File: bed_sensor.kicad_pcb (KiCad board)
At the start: 2 copper layers, 41 x 36 mm, 32 parts, among them J1 Conn_01x02, J2 Conn_01x06, J3 ISP, J4 Conn_01x02, Q1 2N2219, SW1 SW_SPST, U1 MIC5205-3.3, U2 MPU-9250, U5 CFAH0802D-YYH-JP, U6 ATMEGA328-AU, Y1 Crystal_GND2

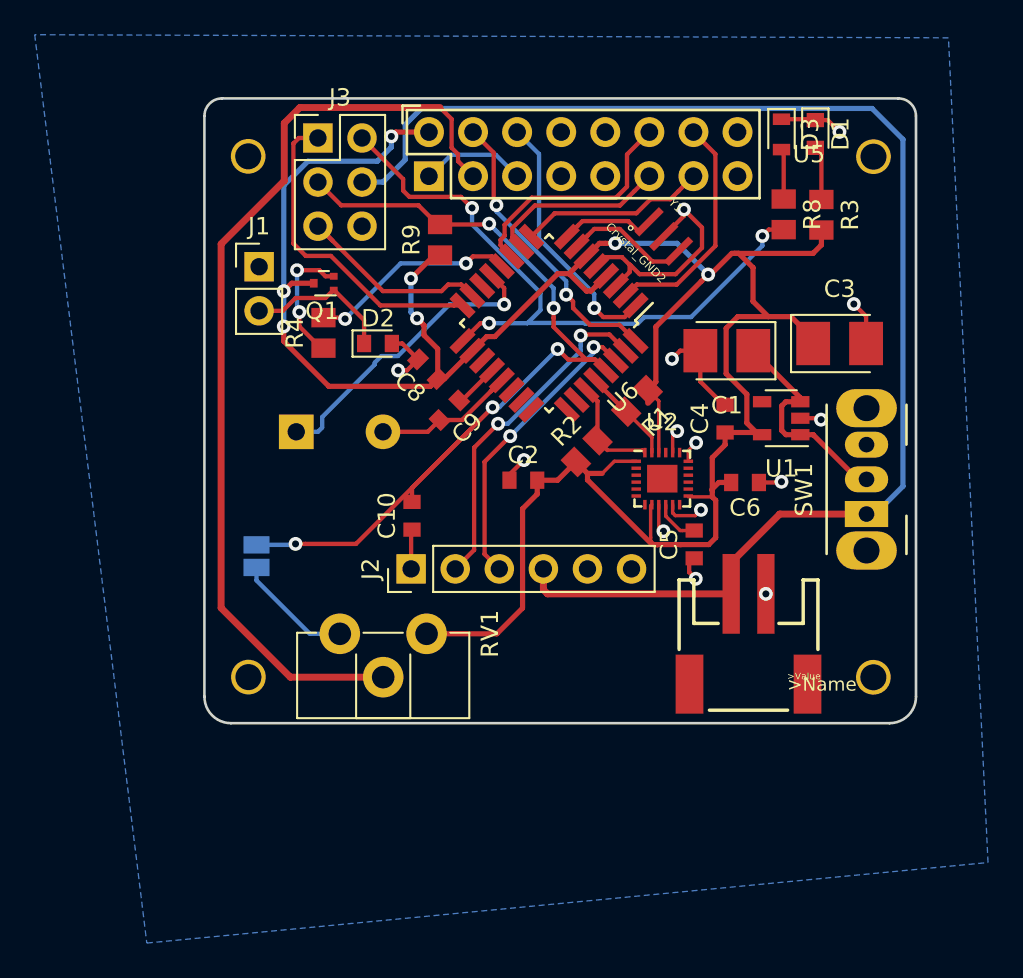
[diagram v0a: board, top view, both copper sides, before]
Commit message: added SD card
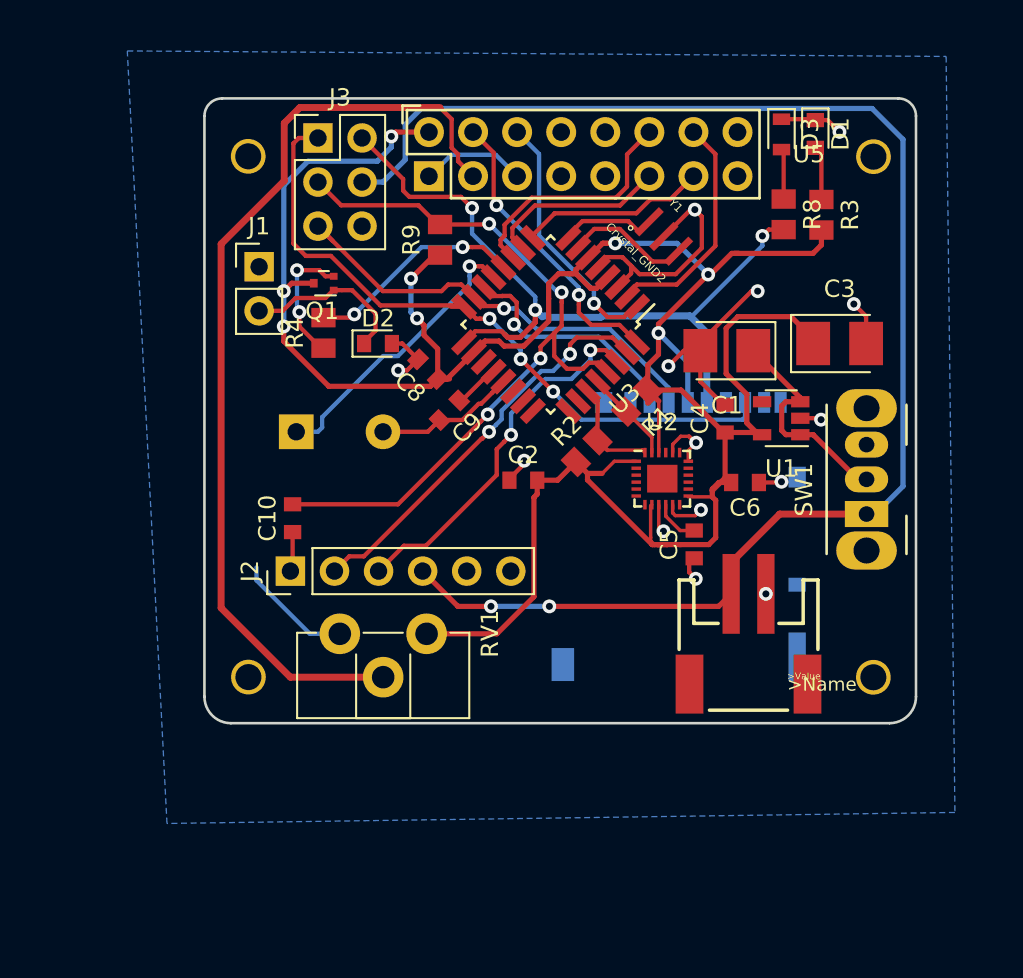
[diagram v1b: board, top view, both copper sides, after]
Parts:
- removed JP1: Jumper_NO_Small, Jumper:SolderJumper-2_P1.3mm_Open_Pad1.0x1.5mm
- removed U6: ATMEGA328-AU, Housings_QFP:TQFP-32_7x7mm_Pitch0.8mm
- added J5: DM3AT-SF-PEJM5, components:HRS_DM3AT-SF-PEJM5, B.Cu at (144.0, 104.0)
- added U3: ATMEGA328-AU, Package_QFP:TQFP-32_7x7mm_P0.8mm, F.Cu at (136.2, 99.5)
- moved J2 6.96 mm to (121.2, 113.7)
- moved C10 6.88 mm to (121.3, 110.7)
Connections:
- net /Ardunio/SCK renamed SCK
- J3 pad 1: /Ardunio/MISO -> MISO
- J3 pad 5: /Ardunio/MOSI -> MOSI
- U1 pad 4: Net-(U1-Pad4) -> (no net)
- U2 pad 12: Net-(U2-Pad12) -> (no net)
- U2 pad 21: Net-(U2-Pad21) -> (no net)
- U2 pad 7: Net-(U2-Pad7) -> (no net)
- U5 pad 10: Net-(U5-Pad10) -> (no net)
- U5 pad 15: Net-(U5-Pad15) -> (no net)
- U5 pad 16: Net-(U5-Pad16) -> (no net)
- U5 pad 7: Net-(U5-Pad7) -> (no net)
- U5 pad 8: Net-(U5-Pad8) -> (no net)
- U5 pad 9: Net-(U5-Pad9) -> (no net)
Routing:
- net MISO: track 0.00 -> 39.4 mm, vias 0 -> 3
- net MOSI: track 0.00 -> 26.3 mm, vias 0 -> 1
- net /Ardunio/MISO: track 18.5 -> 0.00 mm
- net CS: track 0.00 -> 13.8 mm, vias 0 -> 1
- net /Ardunio/MOSI: track 12.1 -> 0.00 mm
- net +3V3: track 145.8 -> 154.7 mm, vias 7 -> 8
- net /Ardunio/RESET: track 52.5 -> 43.9 mm, vias 5 -> 4
- net VCC: track 80.5 -> 87.3 mm, vias 0 -> 2
- net GND: track 63.8 -> 69.8 mm
- net SCK: track 38.7 -> 44.2 mm
- net /Ardunio/RX1: track 17.3 -> 21.3 mm
- net /Ardunio/TX0: track 19.8 -> 23.3 mm
- net Net-(D2-Pad1): track 8.61 -> 9.76 mm
- net Buzzer: track 17.4 -> 16.4 mm

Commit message: added toggle button to side of board
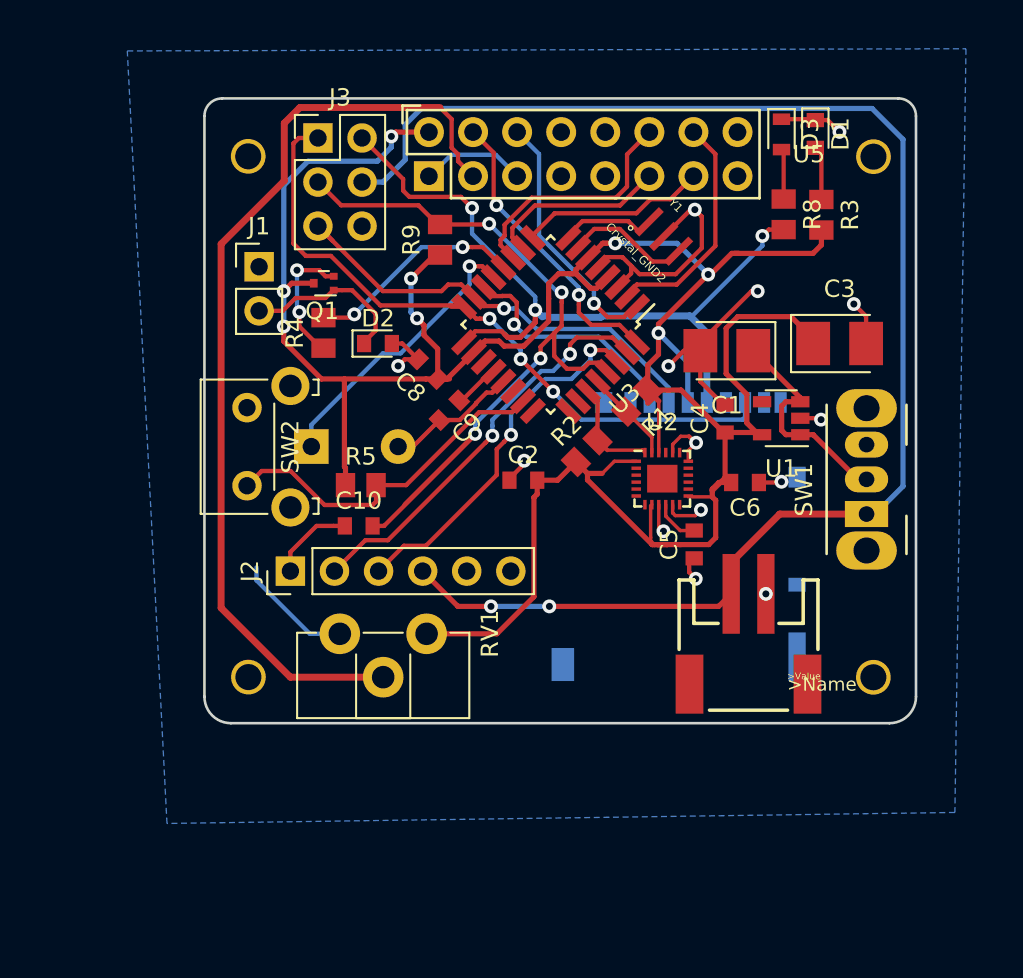
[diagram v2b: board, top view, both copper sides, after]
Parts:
- added R5: 10k, Resistor_SMD:R_0805_2012Metric, F.Cu at (125.2, 108.8)
- added SW2: SW_Push_Open, Button_Switch_THT:SW_Tactile_SKHH_Angled, F.Cu at (118.7, 108.8)
- moved C10 3.84 mm to (125.1, 111.1), turned to 0 degrees
- moved BZ1 1.22 mm to (124.9, 106.6)
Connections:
- U3 pad 23: (no net) -> MODE_SWITCH
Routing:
- net MODE_SWITCH: track 0.00 -> 20.1 mm
- net +3V3: track 154.7 -> 160.5 mm
- net /Ardunio/DTR: track 2.30 -> 4.86 mm
- net /Ardunio/RESET: track 43.9 -> 45.8 mm
- net Buzzer: track 16.4 -> 17.5 mm
- net GND: track 69.8 -> 69.2 mm

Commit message: flipped screen
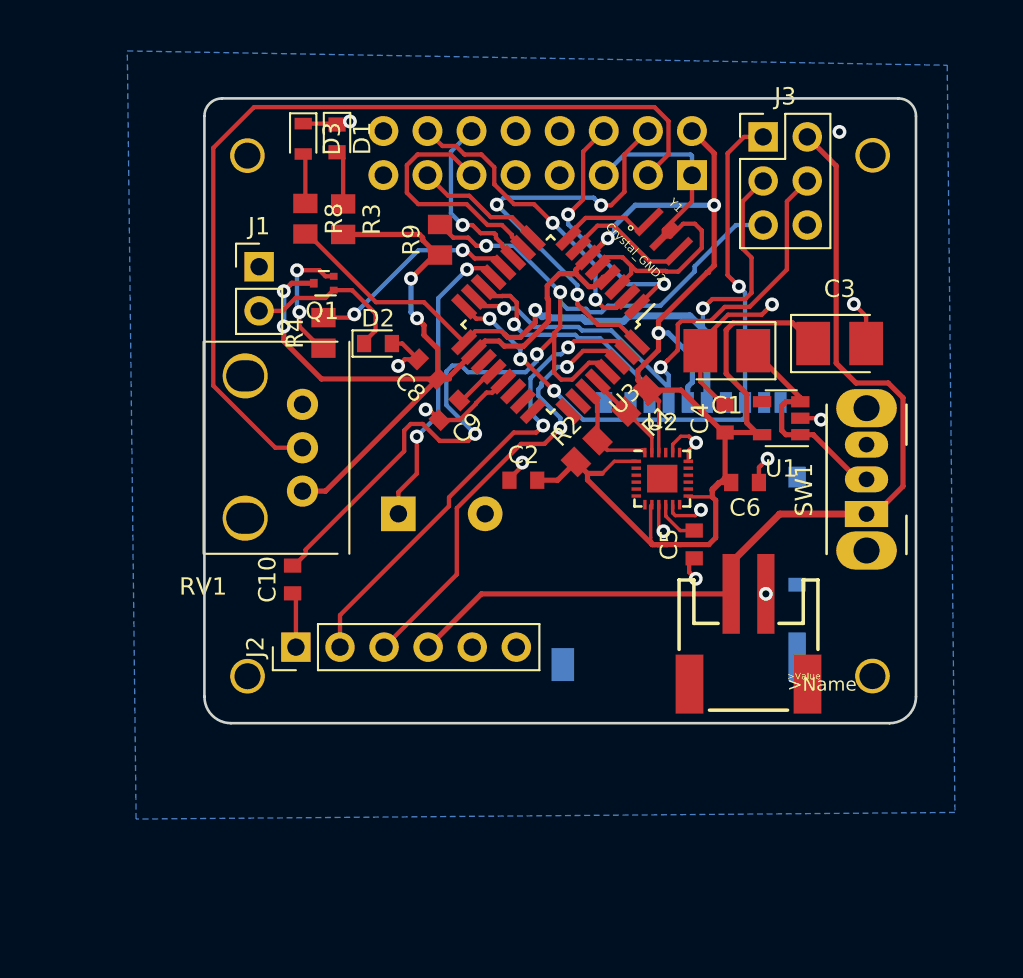
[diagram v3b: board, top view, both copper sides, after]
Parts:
- removed R5: 10k, Resistor_SMD:R_0805_2012Metric
- removed SW2: SW_Push_Open, Button_Switch_THT:SW_Tactile_SKHH_Angled
- RV1: footprint Potentiometers:Potentiometer_Trimmer_ACP_CA9h2.5_Vertical_Px2.5mm_Py5.0mm -> components:BI P090L-02F25BR10K
- U5: moved to B.Cu
- moved U5 36.1 mm to (118.7, 89.8), turned to 180 degrees
- moved D1 27.6 mm to (123.9, 88.8)
- moved D3 27.6 mm to (121.9, 88.8)
- moved R3 27.6 mm to (124.2, 93.5)
- moved R8 27.6 mm to (122.0, 93.4)
- moved J3 25.7 mm to (148.4, 88.7)
- moved RV1 12.4 mm to (118.6, 110.7), turned to 180 degrees
- moved BZ1 6.34 mm to (129.9, 110.4)
- moved C10 4.90 mm to (121.3, 114.2), turned to 90 degrees
- moved J2 4.39 mm to (121.5, 118.1)
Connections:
- J3 pad 2: SCK -> VCC
- J3 pad 3: /Ardunio/RESET -> SCK
- J3 pad 4: VCC -> MOSI
- J3 pad 5: MOSI -> /Ardunio/RESET
- U3 pad 23: MODE_SWITCH -> (no net)
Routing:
- net VCC: track 87.3 -> 56.3 mm, vias 2 -> 0
- net MODE_SWITCH: track 20.1 -> 0.00 mm
- net +3V3: track 160.5 -> 142.2 mm, vias 8 -> 7
- net /Ardunio/RESET: track 45.8 -> 59.4 mm
- net GND: track 69.2 -> 61.5 mm
- net RS: track 16.9 -> 24.2 mm, vias 2 -> 3
- net MOSI: track 26.3 -> 32.5 mm, vias 1 -> 2
- net /Ardunio/RX1: track 21.3 -> 26.3 mm
- net /Ardunio/TX0: track 23.5 -> 28.1 mm
- net DB7: track 13.4 -> 17.7 mm, vias 0 -> 2
- net DB5: track 13.8 -> 10.1 mm, vias 0 -> 1
- net DB4: track 10.4 -> 14.1 mm
- net DB6: track 10.8 -> 7.57 mm
- net Net-(RV1-Pad2): track 54.5 -> 51.5 mm
- net MISO: track 39.4 -> 37.3 mm, vias 3 -> 4
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
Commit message: cleaned up board
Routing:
- net /Ardunio/RESET: track 59.4 -> 55.0 mm
- net /Ardunio/RX1: track 26.3 -> 27.9 mm

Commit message: tweaked layout
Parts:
- BZ1: moved to F.Cu
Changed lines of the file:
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@@
       (drillshape 0)
       (scaleselection 1)
-      (outputdirectory ../../Downloads/bed_sensor_pcb/))
+      (outputdirectory ../../Downloads/bed_sensor_1_3/))
   )
   (net 0 "")
@@
     (pad 13 thru_hole oval (at -10.374 -1.123 180) (size 1.7272 1.7272) (drill 1.016) (layers *.Cu F.SilkS B.Mask)
       (net 23 DB6))
-    (pad 14 thru_hole oval (at -10.374 1.417 180) (size 1.7272 1.7272) (drill 1.016) (layers *.Cu F.SilkS B.Mask)
+    (pad 14 thru_hole oval (at -10.374 1.417 180) (size 1.7272 1.7272) (drill 1.016) (layers *.Cu *.SilkS *.Mask)
       (net 22 DB7))
-    (pad 16 thru_hole oval (at -7.834 1.417 180) (size 1.7272 1.7272) (drill 1.016) (layers *.Cu F.SilkS B.Mask))
+    (pad 16 thru_hole oval (at -7.834 1.417 180) (size 1.7272 1.7272) (drill 1.016) (layers *.Cu *.SilkS *.Mask))
     (pad 15 thru_hole oval (at -7.834 -1.123 180) (size 1.7272 1.7272) (drill 1.016) (layers *.Cu F.SilkS B.Mask))
   )
-  (module components:PS1240P02BT (layer B.Cu)
+  (module components:PS1240P02BT (layer F.Cu)
     (at 129.901001 110.435)
     (descr "Generic Buzzer, D12mm height 9.5mm with RM7.6mm")
     (tags buzzer)
-    (fp_text reference BZ1 (at -0.01 7.2) (layer B.SilkS)
-      (effects (font (size 1 1) (thickness 0.15)) (justify mirror))
-    )
-    (fp_text value Buzzer (at -0.01 -7.4) (layer B.Fab)
-      (effects (font (size 1 1) (thickness 0.15)) (justify mirror))
-    )
-    (fp_circle (center 0 0) (end 6.1 0) (layer B.SilkS) (width 0.15))
-    (fp_text user + (at -3.82 2.54) (layer B.Fab)
-      (effects (font (size 1 1) (thickness 0.15)) (justify mirror))
-    )
-    (fp_text user + (at -3.82 2.54) (layer B.SilkS)
-      (effects (font (size 1 1) (thickness 0.15)) (justify mirror))
-    )
-    (fp_text user %R (at -0.01 4) (layer B.Fab)
-      (effects (font (size 1 1) (thickness 0.15)) (justify mirror))
+    (fp_text reference BZ1 (at -0.01 -7.2) (layer F.SilkS)
+      (effects (font (size 1 1) (thickness 0.15)))
+    )
+    (fp_text value Buzzer (at -0.01 7.4) (layer F.Fab)
+      (effects (font (size 1 1) (thickness 0.15)))
+    )
+    (fp_circle (center 0 0) (end 6.1 0) (layer F.SilkS) (width 0.15))
+    (fp_text user + (at -3.82 -2.54) (layer F.Fab)
+      (effects (font (size 1 1) (thickness 0.15)))
+    )
+    (fp_text user + (at -3.82 -2.54) (layer F.SilkS)
+      (effects (font (size 1 1) (thickness 0.15)))
+    )
+    (fp_text user %R (at -0.01 -4) (layer F.Fab)
+      (effects (font (size 1 1) (thickness 0.15)))
     )
     (pad 1 thru_hole rect (at -2.5 0) (size 2 2) (drill 1) (layers *.Cu *.Mask)
@@
   (segment (start 130.4269 89.569101) (end 130.4269 93.124897) (width 0.25) (layer B.Cu) (net 25))
   (segment (start 130.4269 93.124897) (end 131.100003 93.798) (width 0.25) (layer B.Cu) (net 25))
+  (segment (start 147.387541 98.061966) (end 145.481198 98.061966) (width 0.25) (layer F.Cu) (net 26))
+  (segment (start 147.747503 97.702004) (end 147.387541 98.061966) (width 0.25) (layer F.Cu) (net 26))
+  (segment (start 147.747503 96.936002) (end 147.747503 97.702004) (width 0.25) (layer F.Cu) (net 26))
+  (segment (start 146.959001 96.1475) (end 147.747503 96.936002) (width 0.25) (layer F.Cu) (net 26))
+  (segment (start 148.419501 91.258) (end 146.959001 92.7185) (width 0.25) (layer F.Cu) (net 26))
+  (segment (start 145.481198 98.061966) (end 145.345673 98.197491) (width 0.25) (layer F.Cu) (net 26))
+  (segment (start 146.959001 92.7185) (end 146.959001 96.1475) (width 0.25) (layer F.Cu) (net 26))
+  (segment (start 145.345673 98.197491) (end 144.945674 98.59749) (width 0.25) (layer F.Cu) (net 26))
   (segment (start 144.361186 99.1955) (end 139.380882 99.1955) (width 0.4) (layer B.Cu) (net 26))
   (segment (start 145.181001 100.015315) (end 144.361186 99.1955) (width 0.4) (layer B.Cu) (net 26))
@@
   (segment (start 145.181001 98.832817) (end 144.945674 98.59749) (width 0.25) (layer B.Cu) (net 26))
   (segment (start 145.174501 100.5925) (end 145.181001 100.586) (width 0.4) (layer B.Cu) (net 26))
-  (segment (start 147.387541 98.061966) (end 145.481198 98.061966) (width 0.25) (layer F.Cu) (net 26))
-  (segment (start 145.481198 98.061966) (end 145.345673 98.197491) (width 0.25) (layer F.Cu) (net 26))
-  (segment (start 145.345673 98.197491) (end 144.945674 98.59749) (width 0.25) (layer F.Cu) (net 26))
-  (segment (start 147.747503 97.702004) (end 147.387541 98.061966) (width 0.25) (layer F.Cu) (net 26))
-  (segment (start 147.747503 95.672498) (end 147.747503 97.702004) (width 0.25) (layer F.Cu) (net 26))
-  (segment (start 147.239503 95.164498) (end 147.747503 95.672498) (width 0.25) (layer F.Cu) (net 26))
-  (segment (start 147.239503 92.437998) (end 147.239503 95.164498) (width 0.25) (layer F.Cu) (net 26))
-  (segment (start 148.419501 91.258) (end 147.239503 92.437998) (width 0.25) (layer F.Cu) (net 26))
   (segment (start 126.110001 98.243) (end 128.877779 98.243) (width 0.25) (layer F.Cu) (net 26))
   (segment (start 128.877779 98.243) (end 131.187037 100.552258) (width 0.25) (layer F.Cu) (net 26) (status 20))
@@
   (via (at 147.022493 97.336953) (size 0.8) (drill 0.4) (layers F.Cu B.Cu) (net 30))
   (segment (start 122.041001 94.314) (end 121.901001 94.314) (width 0.25) (layer F.Cu) (net 26) (status 30))
+  (segment (start 145.399322 99.3225) (end 143.702499 99.3225) (width 0.25) (layer F.Cu) (net 31))
+  (segment (start 150.959501 91.258) (end 149.689501 92.528) (width 0.25) (layer F.Cu) (net 31))
+  (segment (start 146.209845 98.511977) (end 145.399322 99.3225) (width 0.25) (layer F.Cu) (net 31))
+  (segment (start 147.637439 98.511977) (end 146.209845 98.511977) (width 0.25) (layer F.Cu) (net 31))
+  (segment (start 143.498 101.005501) (end 142.914 101.589501) (width 0.25) (layer F.Cu) (net 31))
+  (segment (start 149.689501 96.459915) (end 147.637439 98.511977) (width 0.25) (layer F.Cu) (net 31))
+  (segment (start 149.689501 92.528) (end 149.689501 96.459915) (width 0.25) (layer F.Cu) (net 31))
+  (segment (start 143.702499 99.3225) (end 143.498 99.526999) (width 0.25) (layer F.Cu) (net 31))
+  (segment (start 143.498 99.526999) (end 143.498 101.005501) (width 0.25) (layer F.Cu) (net 31))
+  (segment (start 142.914 101.589501) (end 142.514001 101.9895) (width 0.25) (layer F.Cu) (net 31))
   (segment (start 139.677091 99.87409) (end 137.926601 99.87409) (width 0.25) (layer B.Cu) (net 31))
   (segment (start 142.974501 104.0215) (end 142.974501 103.1715) (width 0.25) (layer B.Cu) (net 31))
@@
   (segment (start 132.282612 98.465852) (end 133.138976 98.465852) (width 0.25) (layer F.Cu) (net 31))
   (segment (start 133.138976 98.465852) (end 133.287876 98.614752) (width 0.25) (layer F.Cu) (net 31))
-  (segment (start 143.498 99.526999) (end 143.498 101.005501) (width 0.25) (layer F.Cu) (net 31))
-  (segment (start 143.702499 99.3225) (end 143.498 99.526999) (width 0.25) (layer F.Cu) (net 31))
-  (segment (start 150.959501 91.258) (end 149.7845 92.433001) (width 0.25) (layer F.Cu) (net 31))
-  (segment (start 149.7845 92.433001) (end 149.7845 96.364916) (width 0.25) (layer F.Cu) (net 31))
-  (segment (start 147.637439 98.511977) (end 146.209845 98.511977) (width 0.25) (layer F.Cu) (net 31))
-  (segment (start 146.209845 98.511977) (end 145.399322 99.3225) (width 0.25) (layer F.Cu) (net 31))
-  (segment (start 149.7845 96.364916) (end 147.637439 98.511977) (width 0.25) (layer F.Cu) (net 31))
-  (segment (start 143.498 101.005501) (end 142.914 101.589501) (width 0.25) (layer F.Cu) (net 31))
-  (segment (start 142.914 101.589501) (end 142.514001 101.9895) (width 0.25) (layer F.Cu) (net 31))
-  (segment (start 145.399322 99.3225) (end 143.702499 99.3225) (width 0.25) (layer F.Cu) (net 31))
   (segment (start 142.514001 101.9895) (end 142.974501 102.45) (width 0.25) (layer B.Cu) (net 31))
   (segment (start 142.974501 102.45) (end 142.974501 104.0215) (width 0.25) (layer B.Cu) (net 31) (status 20))
